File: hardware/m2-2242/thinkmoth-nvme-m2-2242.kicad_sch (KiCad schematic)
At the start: 18 parts, among them J2 ExpressCard, J3 MDT180M03001, U1 GL823K-HCY04

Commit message: updates
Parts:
- added R3, R4: 0r, Resistor_SMD:R_0402_1005Metric, symbol Device:R
- R1, R2: value 680r -> 4k
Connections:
- net PCIe_LED: now also R3.2; no longer R1.2
- net SD_LED: now also R4.2; no longer R2.2
- new net PCIe_LED_S: R1.2, R3.1
- new net SD_LED_S: R2.2, R4.1
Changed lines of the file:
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@@
 		)
 	)
-	(global_label "PCIe_LED"
-		(shape input)
-		(at 118.11 153.67 0)
-		(fields_autoplaced yes)
-		(effects
-			(font
-				(size 1.27 1.27)
-			)
-			(justify left)
-		)
-		(property "Intersheetrefs" "${INTERSHEET_REFS}"
-			(at 129.7433 153.67 0)
-			(effects
-				(font
-					(size 1.27 1.27)
-				)
-				(justify left)
-				(hide yes)
-			)
-		)
-	)
 	(global_label "PCIe_CLK_P"
 		(shape input)
@@
 		)
 	)
+	(global_label "SD_LED_S"
+		(shape input)
+		(at 118.11 165.1 0)
+		(fields_autoplaced yes)
+		(effects
+			(font
+				(size 1.27 1.27)
+			)
+			(justify left)
+		)
+		(property "Intersheetrefs" "${INTERSHEET_REFS}"
+			(at 130.1665 165.1 0)
+			(effects
+				(font
+					(size 1.27 1.27)
+				)
+				(justify left)
+				(hide yes)
+			)
+		)
+	)
 	(global_label "SD_CLK"
 		(shape input)
@@
 		)
 	)
-	(global_label "SD_LED"
+	(global_label "PCIe_RX_P"
 		(shape input)
-		(at 118.11 165.1 0)
+		(at 102.87 81.28 180)
 		(fields_autoplaced yes)
 		(effects
@@
 				(size 1.27 1.27)
 			)
-			(justify left)
+			(justify right)
 		)
 		(property "Intersheetrefs" "${INTERSHEET_REFS}"
-			(at 127.9894 165.1 0)
+			(at 89.9667 81.28 0)
 			(effects
 				(font
 					(size 1.27 1.27)
 				)
-				(justify left)
+				(justify right)
 				(hide yes)
 			)
 		)
 	)
-	(global_label "PCIe_RX_P"
+	(global_label "3V3_F"
 		(shape input)
-		(at 102.87 81.28 180)
+		(at 156.21 147.32 90)
 		(fields_autoplaced yes)
 		(effects
@@
 				(size 1.27 1.27)
 			)
-			(justify right)
+			(justify left)
 		)
 		(property "Intersheetrefs" "${INTERSHEET_REFS}"
-			(at 89.9667 81.28 0)
+			(at 156.21 138.771 90)
 			(effects
 				(font
 					(size 1.27 1.27)
 				)
-				(justify right)
+				(justify left)
 				(hide yes)
 			)
 		)
 	)
-	(global_label "3V3_F"
+	(global_label "USB_P"
 		(shape input)
-		(at 156.21 147.32 90)
+		(at 187.96 90.17 0)
 		(fields_autoplaced yes)
 		(effects
@@
 		)
 		(property "Intersheetrefs" "${INTERSHEET_REFS}"
-			(at 156.21 138.771 90)
+			(at 196.9928 90.17 0)
 			(effects
 				(font
@@
 		)
 	)
-	(global_label "USB_P"
+	(global_label "PCIe_LED_S"
 		(shape input)
-		(at 187.96 90.17 0)
+		(at 59.69 95.25 180)
 		(fields_autoplaced yes)
 		(effects
@@
 				(size 1.27 1.27)
 			)
-			(justify left)
+			(justify right)
 		)
 		(property "Intersheetrefs" "${INTERSHEET_REFS}"
-			(at 196.9928 90.17 0)
+			(at 45.8796 95.25 0)
 			(effects
 				(font
 					(size 1.27 1.27)
 				)
-				(justify left)
+				(justify right)
 				(hide yes)
 			)
@@
 		)
 	)
+	(global_label "PCIe_LED_S"
+		(shape input)
+		(at 118.11 153.67 0)
+		(fields_autoplaced yes)
+		(effects
+			(font
+				(size 1.27 1.27)
+			)
+			(justify left)
+		)
+		(property "Intersheetrefs" "${INTERSHEET_REFS}"
+			(at 131.9204 153.67 0)
+			(effects
+				(font
+					(size 1.27 1.27)
+				)
+				(justify left)
+				(hide yes)
+			)
+		)
+	)
 	(global_label "PCIe_TX_C_P"
 		(shape input)
@@
 		)
 	)
+	(global_label "SD_LED"
+		(shape input)
+		(at 67.31 100.33 0)
+		(fields_autoplaced yes)
+		(effects
+			(font
+				(size 1.27 1.27)
+			)
+			(justify left)
+		)
+		(property "Intersheetrefs" "${INTERSHEET_REFS}"
+			(at 77.1894 100.33 0)
+			(effects
+				(font
+					(size 1.27 1.27)
+				)
+				(justify left)
+				(hide yes)
+			)
+		)
+	)
 	(global_label "SD_CMD"
 		(shape input)
@@
 		)
 	)
+	(global_label "PCIe_LED"
+		(shape input)
+		(at 67.31 95.25 0)
+		(fields_autoplaced yes)
+		(effects
+			(font
+				(size 1.27 1.27)
+			)
+			(justify left)
+		)
+		(property "Intersheetrefs" "${INTERSHEET_REFS}"
+			(at 78.9433 95.25 0)
+			(effects
+				(font
+					(size 1.27 1.27)
+				)
+				(justify left)
+				(hide yes)
+			)
+		)
+	)
 	(global_label "SD_DAT2"
 		(shape input)
@@
 		)
 	)
+	(global_label "SD_LED_S"
+		(shape input)
+		(at 59.69 100.33 180)
+		(fields_autoplaced yes)
+		(effects
+			(font
+				(size 1.27 1.27)
+			)
+			(justify right)
+		)
+		(property "Intersheetrefs" "${INTERSHEET_REFS}"
+			(at 47.6335 100.33 0)
+			(effects
+				(font
+					(size 1.27 1.27)
+				)
+				(justify right)
+				(hide yes)
+			)
+		)
+	)
 	(global_label "CLKREQ"
 		(shape input)
@@
 			)
 		)
-		(property "Value" "680r"
+		(property "Value" "4k"
 			(at 115.57 162.56 90)
 			(effects
@@
 			)
 		)
-		(property "Value" "680r"
+		(property "Value" "4k"
 			(at 115.57 151.13 90)
 			(effects
@@
 	)
 	(symbol
+		(lib_id "Device:R")
+		(at 63.5 100.33 90)
+		(unit 1)
+		(exclude_from_sim no)
+		(in_bom yes)
+		(on_board yes)
+		(dnp no)
+		(property "Reference" "R4"
+			(at 63.5 102.87 90)
+			(effects
+				(font
+					(size 1.27 1.27)
+				)
+			)
+		)
+		(property "Value" "0r"
+			(at 63.5 105.41 90)
+			(effects
+				(font
+					(size 1.27 1.27)
+				)
+			)
+		)
+		(property "Footprint" "Resistor_SMD:R_0402_1005Metric"
+			(at 63.5 102.108 90)
+			(effects
+				(font
+					(size 1.27 1.27)
+				)
+				(hide yes)
+			)
+		)
+		(property "Datasheet" "~"
+			(at 63.5 100.33 0)
+			(effects
+				(font
+					(size 1.27 1.27)
+				)
+				(hide yes)
+			)
+		)
+		(property "Description" "Resistor"
+			(at 63.5 100.33 0)
+			(effects
+				(font
+					(size 1.27 1.27)
+				)
+				(hide yes)
+			)
+		)
+		(pin "2"
+		)
+		(pin "1"
+		)
+		(instances
+			(project "thinkmoth-nvme-m2-2242"
+				(path "/555b1918-907f-4888-b85a-a9dd6e2461f8"
+					(reference "R4")
+					(unit 1)
+				)
+			)
+		)
+	)
+	(symbol
 		(lib_id "Mechanical:MountingHole_Pad")
 		(at 48.26 156.21 0)
@@
 					(unit 1)
 				)
+			)
+		)
+	)
+	(symbol
+		(lib_id "Device:R")
+		(at 63.5 95.25 90)
+		(unit 1)
+		(exclude_from_sim no)
+		(in_bom yes)
+		(on_board yes)
+		(dnp no)
+		(fields_autoplaced yes)
+		(property "Reference" "R3"
+			(at 63.5 88.9 90)
+			(effects
+				(font
+					(size 1.27 1.27)
+				)
+			)
+		)
+		(property "Value" "0r"
+			(at 63.5 91.44 90)
+			(effects
+				(font
+					(size 1.27 1.27)
+				)
+			)
+		)
+		(property "Footprint" "Resistor_SMD:R_0402_1005Metric"
+			(at 63.5 97.028 90)
+			(effects
+				(font
+					(size 1.27 1.27)
+				)
+				(hide yes)
+			)
+		)
+		(property "Datasheet" "~"
+			(at 63.5 95.25 0)
+			(effects
+				(font
+					(size 1.27 1.27)
+				)
+				(hide yes)
+			)
+		)
+		(property "Description" "Resistor"
+			(at 63.5 95.25 0)
+			(effects
+				(font
+					(size 1.27 1.27)
+				)
+				(hide yes)
+			)
+		)
+		(pin "2"
+		)
+		(pin "1"
+		)
+		(instances
+			(project ""
+				(path "/555b1918-907f-4888-b85a-a9dd6e2461f8"
+					(reference "R3")
+					(unit 1)
+				)

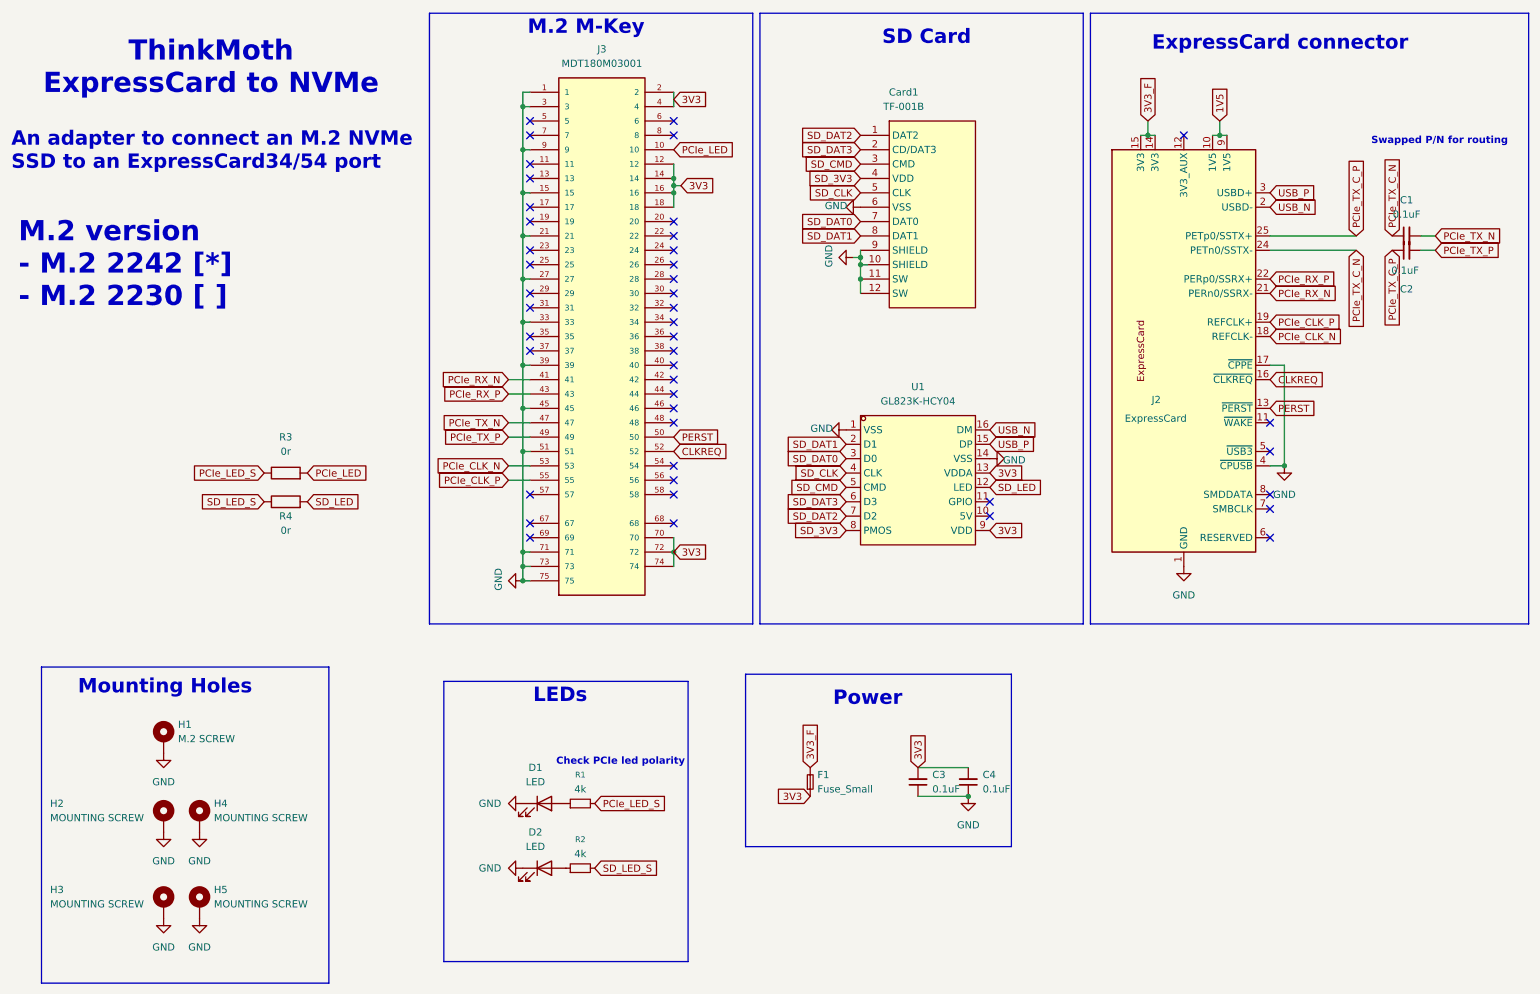
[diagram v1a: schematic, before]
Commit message: combined m.2 2230 and 2242 design, wip
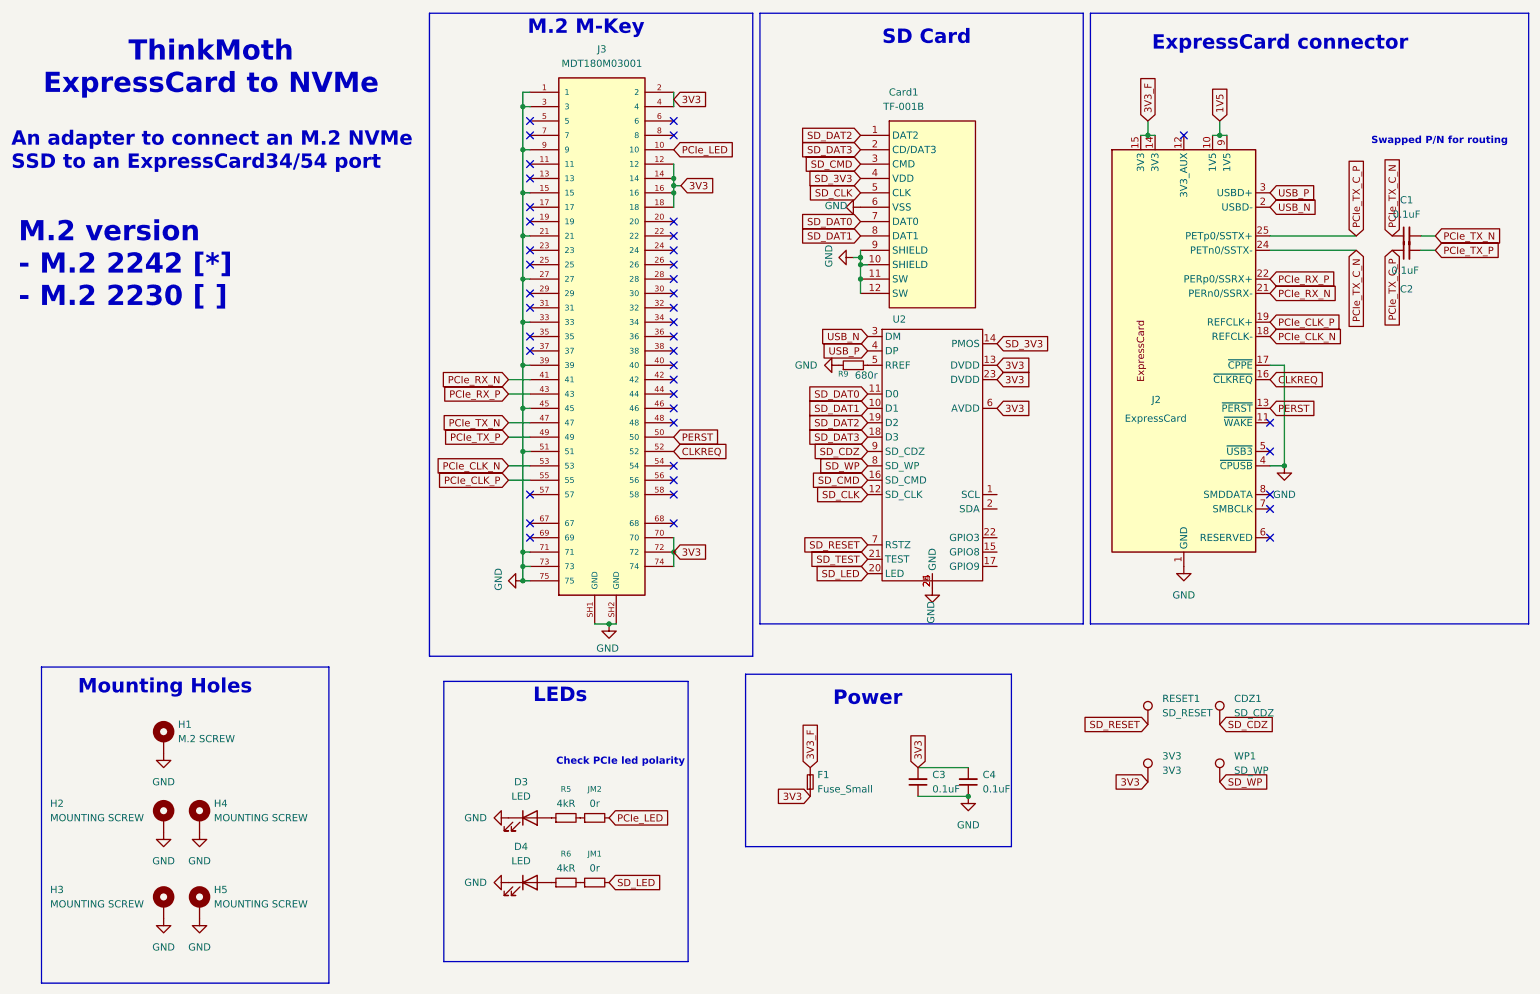
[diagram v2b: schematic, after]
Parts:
- removed D1, D2: LED, LED_SMD:LED_0603_1608Metric, symbol Device:LED
- removed R1, R2: 4k, Resistor_SMD:R_0402_1005Metric, symbol Device:R_Small
- removed R3, R4: 0r, Resistor_SMD:R_0402_1005Metric, symbol Device:R
- removed U1: GL823K-HCY04, GL823K-HCY04:SSOP-16_L4.9-W3.9-P0.64-LS6.0-BL, symbol GL823K-HCY04:GL823K-HCY04
- added 3V3: 3V3, TestPoint:TestPoint_Pad_D1.0mm, symbol Connector:TestPoint
- added CDZ1: SD_CDZ, TestPoint:TestPoint_Pad_D1.0mm, symbol Connector:TestPoint
- added D3, D4: LED, LED_SMD:LED_0603_1608Metric, symbol Device:LED
- added JM1, JM2: 0r, Resistor_SMD:R_0402_1005Metric, symbol Device:R_Small
- added R5, R6: 4kR, Resistor_SMD:R_0402_1005Metric, symbol Device:R_Small
- added R9: 680r, Resistor_SMD:R_0402_1005Metric, symbol Device:R_Small
- added RESET1: SD_RESET, TestPoint:TestPoint_Pad_D1.0mm, symbol Connector:TestPoint
- added U2: ~, Package_DFN_QFN:QFN-24-1EP_4x4mm_P0.5mm_EP2.7x2.6mm_ThermalVias, symbol GL823-B-QFN24:GL823A
- added WP1: SD_WP, TestPoint:TestPoint_Pad_D1.0mm, symbol Connector:TestPoint
- J3: footprint MDT180M03001_2:AMPHENOL_MDT180M03001 -> MDT180M03001:AMPHENOL_MDT180M03001
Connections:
- net 3V3: now also 3V3.1, U2.13 (DVDD), U2.23 (DVDD), U2.6 (AVDD)
- net GND: now also J3.SH1 (GND), J3.SH2 (GND), D3.1 (K), D4.1 (K), R9.1, U2.24 (GND), U2.25 (GND)
- net PCIe_LED: now also JM2.2
- net SD_3V3: now also U2.14 (PMOS)
- net SD_CLK: now also U2.12 (SD_CLK)
- net SD_CMD: now also U2.16 (SD_CMD)
- net SD_DAT0: now also U2.11 (D0)
- net SD_DAT1: now also U2.10 (D1)
- net SD_DAT2: now also U2.19 (D2)
- net SD_DAT3: now also U2.18 (D3)
- net SD_LED: now also JM1.2, U2.20 (LED)
- net USB_N: now also U2.3 (DM)
- net USB_P: now also U2.4 (DP)
- new net: D3.2 (A), R5.1
- new net: JM2.1, R5.2
- new net: R9.2, U2.5 (RREF)
- new net: JM1.1, R6.2
- new net: D4.2 (A), R6.1
- new net SD_CDZ: CDZ1.1, U2.9 (SD_CDZ)
- new net SD_RESET: RESET1.1, U2.7 (RSTZ)
- new net SD_TEST: U2.21 (TEST)
- new net SD_WP: U2.8 (SD_WP), WP1.1
- no-connect marks 44 -> 42
